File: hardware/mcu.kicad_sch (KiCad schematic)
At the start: 54 parts, among them J10 PRPC001DAAN-RC, J11 PRPC006SAAN-RC, J12 PRPC004SAAN-RC, J8 SBH11-NBPC-D05-SM-BK, J9 PRPC006SAAN-RC, U5 AT25SF081B-SSHD-B, U6 MCP9808T-E/MS, U7 STM32L552CET6, Y1 ABS05-32.768KHZ-9-T, Y2 ECS-160-9-37-CKM-TR3

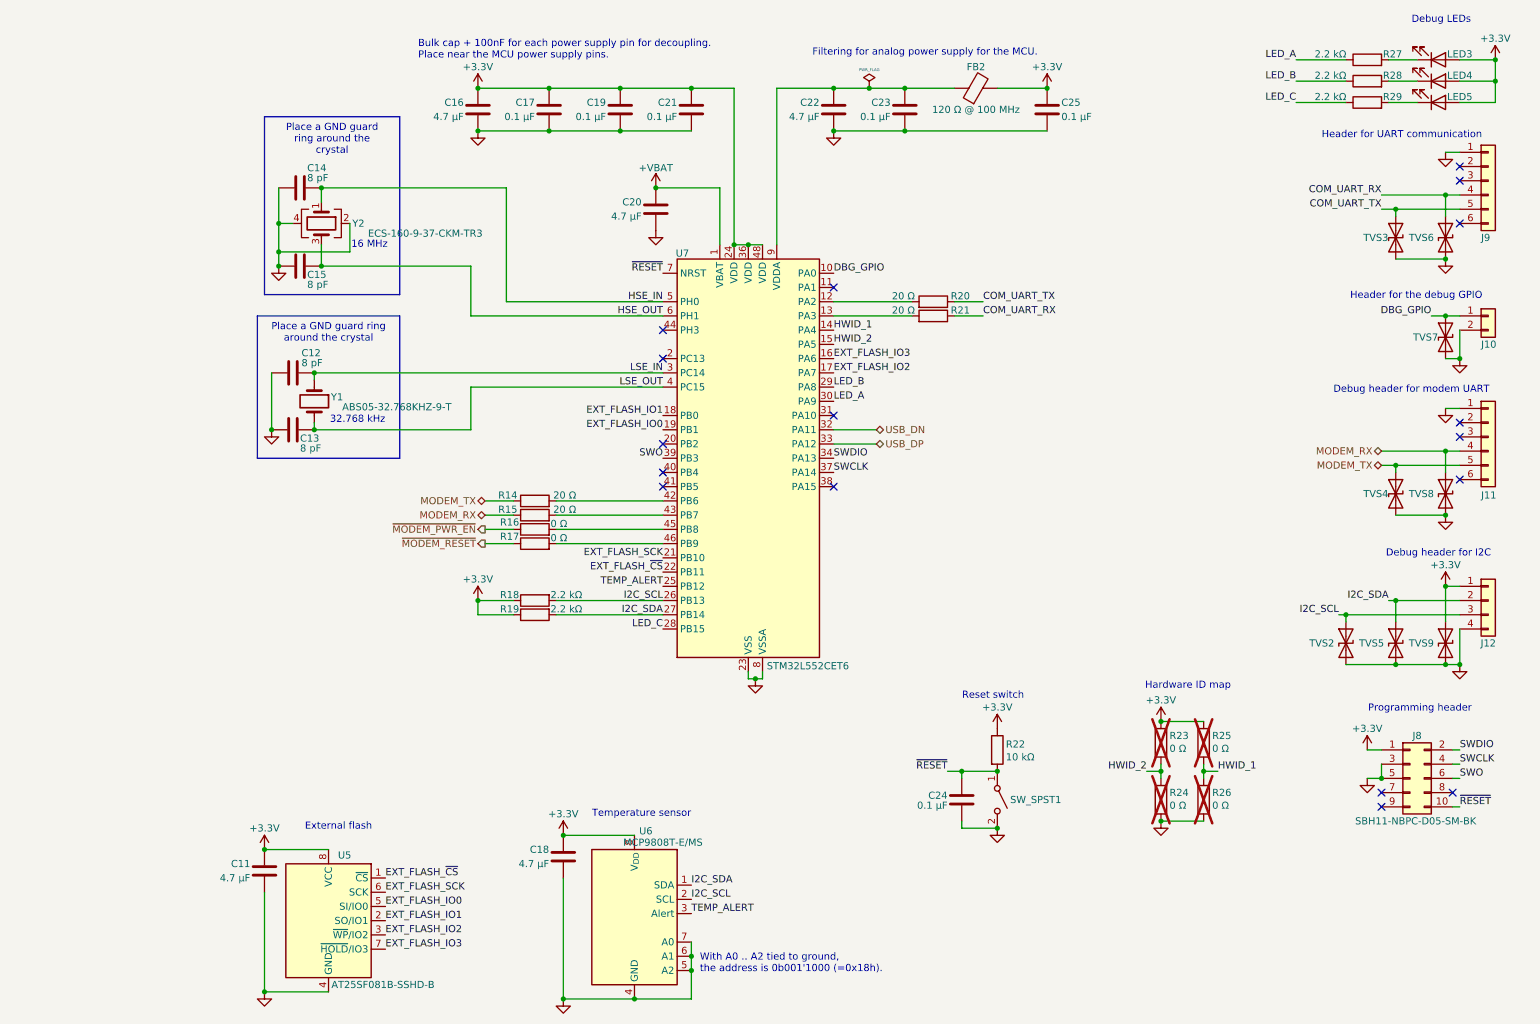
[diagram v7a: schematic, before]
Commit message: HW: Add battery sense, refine schema and components
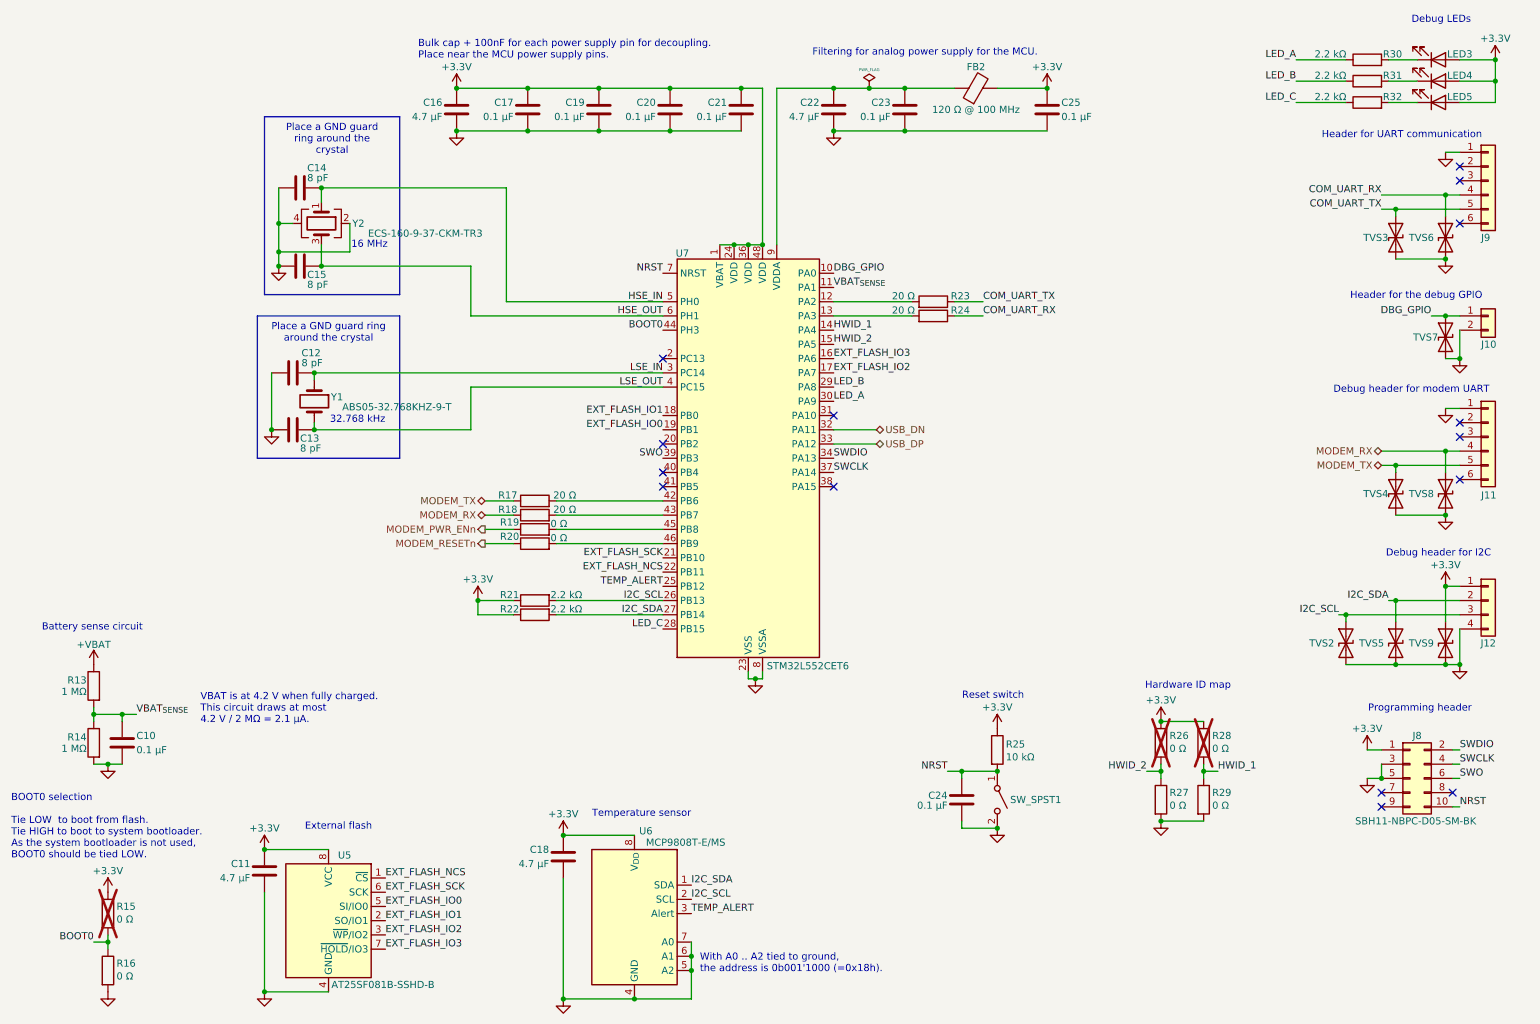
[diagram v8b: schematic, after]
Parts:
- removed C20: 4.7 µF, Capacitor_SMD:C_0805_2012Metric_Pad1.18x1.45mm_HandSolder, symbol Device:C
- added C10, C21: 0.1 µF, Capacitor_SMD:C_0603_1608Metric_Pad1.08x0.95mm_HandSolder, symbol Device:C
- added R13, R14: 1 MΩ, Resistor_SMD:R_0603_1608Metric_Pad0.98x0.95mm_HandSolder, symbol Device:R
- added R15, R16: 0 Ω, Resistor_SMD:R_0603_1608Metric_Pad0.98x0.95mm_HandSolder, symbol Device:R
- C11, C16, C18, C22: footprint Capacitor_SMD:C_0805_2012Metric_Pad1.18x1.45mm_HandSolder -> Capacitor_SMD:C_0603_1608Metric_Pad1.08x0.95mm_HandSolder; Digi-Key Part Number 732-7623-1-ND -> 1276-1044-1-ND; Manufacturer Würth Elektronik -> Samsung Electro-Mechanics; Manufacturer Part Number 885012107013 -> CL10A475KP8NNNC
- R19: renamed from R16; footprint Resistor_SMD:R_0805_2012Metric_Pad1.20x1.40mm_HandSolder -> Resistor_SMD:R_0603_1608Metric_Pad0.98x0.95mm_HandSolder; Digi-Key Part Number 732-560112120002CT-ND -> 732-560112116001CT-ND; Manufacturer Part Number 560112120002 -> 560112116001
- R20: renamed from R17; footprint Resistor_SMD:R_0805_2012Metric_Pad1.20x1.40mm_HandSolder -> Resistor_SMD:R_0603_1608Metric_Pad0.98x0.95mm_HandSolder; Digi-Key Part Number 732-560112120002CT-ND -> 732-560112116001CT-ND; Manufacturer Part Number 560112120002 -> 560112116001
- R26: renamed from R23; footprint Resistor_SMD:R_0805_2012Metric_Pad1.20x1.40mm_HandSolder -> Resistor_SMD:R_0603_1608Metric_Pad0.98x0.95mm_HandSolder; Digi-Key Part Number 732-560112120002CT-ND -> 732-560112116001CT-ND; Manufacturer Part Number 560112120002 -> 560112116001
- R27: renamed from R24; footprint Resistor_SMD:R_0805_2012Metric_Pad1.20x1.40mm_HandSolder -> Resistor_SMD:R_0603_1608Metric_Pad0.98x0.95mm_HandSolder; Digi-Key Part Number 732-560112120002CT-ND -> 732-560112116001CT-ND; Manufacturer Part Number 560112120002 -> 560112116001; now fitted
- R28: renamed from R25; footprint Resistor_SMD:R_0805_2012Metric_Pad1.20x1.40mm_HandSolder -> Resistor_SMD:R_0603_1608Metric_Pad0.98x0.95mm_HandSolder; Digi-Key Part Number 732-560112120002CT-ND -> 732-560112116001CT-ND; Manufacturer Part Number 560112120002 -> 560112116001
- R29: renamed from R26; footprint Resistor_SMD:R_0805_2012Metric_Pad1.20x1.40mm_HandSolder -> Resistor_SMD:R_0603_1608Metric_Pad0.98x0.95mm_HandSolder; Digi-Key Part Number 732-560112120002CT-ND -> 732-560112116001CT-ND; Manufacturer Part Number 560112120002 -> 560112116001; now fitted
- renumbered C21 to C20, R14 to R17, R15 to R18, R18 to R21, R19 to R22, R20 to R23, R21 to R24, R22 to R25, R27 to R30, R28 to R31, R29 to R32
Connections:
- net +3.3V: now also U7.1 (VBAT), C21.1, R15.1
- net +VBAT: now also R13.1; no longer U7.1 (VBAT)
- net GND: now also C10.2, C21.2, R14.2, R16.2
- net VBAT_{SENSE}: now reaches U7.11 (PA1)
- net VBAT_{SENSE}: now also C10.1, R13.2, R14.1
- net BOOT0: now reaches U7.44 (PH3)
- net BOOT0: now also R15.2, R16.1
- net EXT_FLASH_~{CS} renamed EXT_FLASH_NCS
- net ~{MODEM_PWR_EN} renamed MODEM_PWR_ENn
- net ~{MODEM_RESET} renamed MODEM_RESETn
- net ~{RESET} renamed NRST
- no-connect marks 17 -> 15
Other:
- note added: "BOOT0 selection Tie LOW to boot from flash. Tie HIGH to boot to system bootloader. As the system bootloader is not used, BOOT0 should be tied LOW."
- note added: "Battery sense circuit"
- note added: "VBAT is at 4.2 V when fully charged. This circuit draws at most 4.2 V / 2 MΩ = 2.1 µA."
- moved on the sheet: C16, C17, C19, C20
